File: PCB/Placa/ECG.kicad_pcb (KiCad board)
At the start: 2 copper layers, 60.8 x 24 mm, 59 parts, among them P1 A_CONECTOR_DIN, P2 CONN_01X04, P3 CONN_01X04, P7 Shield, U1 INA333, U2 OPA2335, U3 OPA2335, U4 REF5050, U6 INA333, U7 OPA2335, U8 OPA2335, U9 OPA2335

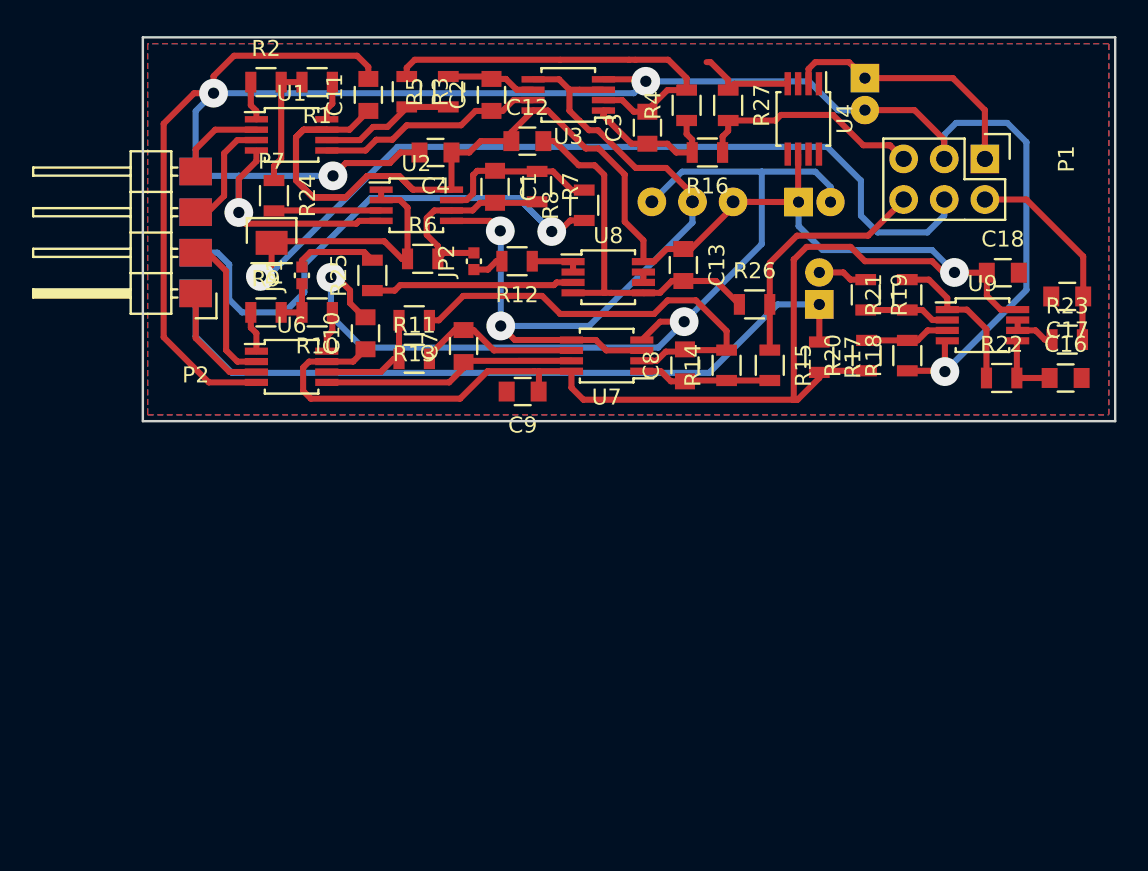
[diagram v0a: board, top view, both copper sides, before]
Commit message: Modifiqué la placa. Le agregué la resistencia para el divisor a la salida del micrófono y cambié la frecuencia del pasabajos a 500Hz aprox, por lo que estuvimos hablando con Mario.
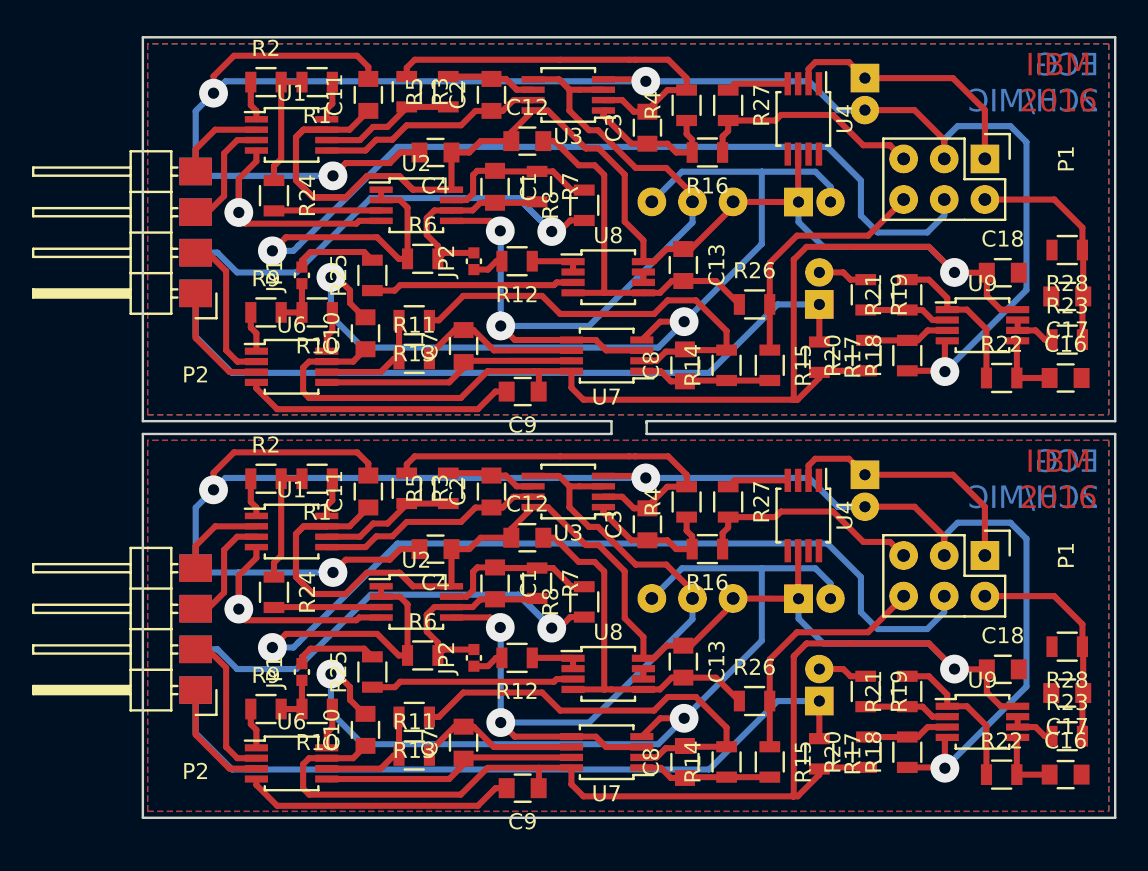
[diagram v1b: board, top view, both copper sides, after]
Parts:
- removed P7: Shield, Pin_Headers:Pin_Header_Straight_1x01
- added C1: 10n, Capacitors_SMD:C_0805, F.Cu at (157.0, 104.7)
- added C10: 0.1u, Capacitors_SMD:C_0805, F.Cu at (148.9, 113.9)
- added C11: 0.1u, Capacitors_SMD:C_0805, F.Cu at (149.1, 99.0)
- added C12: 0.1u, Capacitors_SMD:C_0805, F.Cu at (159.0, 101.9)
- added C13: 0.1u, Capacitors_SMD:C_0805, F.Cu at (168.8, 109.6)
- added C15: 4.7u, Capacitors_ThroughHole:C_Radial_D5_L11_P2, B.Cu at (177.3, 112.1)
- added C16: 0.1u, Capacitors_SMD:C_0805, F.Cu at (192.7, 116.7)
- added C17: 0.1u, Capacitors_SMD:C_0805, F.Cu at (192.8, 111.6)
- added C18: 0.1u, Capacitors_SMD:C_0805, F.Cu at (188.8, 110.1)
- added C2: 1u, Capacitors_SMD:C_0805, F.Cu at (156.8, 99.0)
- added C3: 330n, Capacitors_SMD:C_0805, F.Cu at (166.6, 101.0)
- added C4: 0.1u, Capacitors_SMD:C_0805, F.Cu at (153.3, 102.6)
- added C5: 1u, Capacitors_ThroughHole:C_Radial_D5_L11_P2, B.Cu at (180.2, 98.0)
- added C6: 22u, Capacitors_ThroughHole:C_Radial_D5_L11_P2, B.Cu at (176.0, 105.7)
- added C7: 1u, Capacitors_SMD:C_0805, F.Cu at (155.1, 114.7)
- added C8: 330n, Capacitors_SMD:C_0805, F.Cu at (168.9, 115.9)
- added C9: 0.1u, Capacitors_SMD:C_0805, F.Cu at (158.8, 117.5)
- added JP1: Jumper, jumper_smd:jumper_smd, F.Cu at (144.9, 110.3)
- added JP2: Jumper, jumper_smd:jumper_smd, F.Cu at (155.7, 109.4)
- added P1: A_CONECTOR_DIN, Pin_Headers:Pin_Header_Straight_2x03, F.Cu at (187.7, 103.0)
- added P2: CONN_01X04, Pin_Headers:Pin_Header_Angled_1x04, F.Cu at (138.3, 111.4)
- added P3: CONN_01X04, Pin_Headers:Pin_Header_Angled_1x04, B.Cu at (138.3, 103.8)
- added R1: 12k, Resistors_SMD:R_0805, F.Cu at (145.9, 98.2)
- added R10: 12k, Resistors_SMD:R_0805, F.Cu at (145.9, 112.6)
- added R11: 330k, Resistors_SMD:R_0805, F.Cu at (152.0, 115.5)
- added R12: 10k, Resistors_SMD:R_0805, F.Cu at (158.4, 109.4)
- added R13: 100, Resistors_SMD:R_0805, F.Cu at (152.0, 113.1)
- added R14: 10k, Resistors_SMD:R_0805, F.Cu at (171.5, 115.9)
- added R15: 4,7k, Resistors_SMD:R_0805, F.Cu at (174.2, 115.9)
- added R16: 4,7k, Resistors_SMD:R_0805, F.Cu at (170.3, 102.6)
- added R17: 2.2k, Resistors_SMD:R_0805, F.Cu at (177.3, 115.4)
- added R18: 1.1k, Resistors_SMD:R_0805, F.Cu at (182.8, 115.3)
- added R19: 10k, Resistors_SMD:R_0805, F.Cu at (180.2, 111.5)
- added R2: 12k, Resistors_SMD:R_0805, F.Cu at (142.7, 98.2)
- added R20: 2.2k, Resistors_SMD:R_0805, F.Cu at (180.2, 115.3)
- added R21: 100k, Resistors_SMD:R_0805, F.Cu at (182.8, 111.5)
- added R22: 3.3k, Resistors_SMD:R_0805, F.Cu at (188.7, 116.7)
- added R23: 4.7k, Resistors_SMD:R_0805, F.Cu at (192.8, 114.3)
- added R24: 100k, Resistors_SMD:R_0805, F.Cu at (143.2, 105.3)
- added R25: 100k, Resistors_SMD:R_0805, F.Cu at (149.4, 110.3)
- added R26: 9,1k, Resistors_SMD:R_0805, F.Cu at (173.2, 112.1)
- added R27: 9,1k, Resistors_SMD:R_0805, F.Cu at (171.6, 99.7)
- added R28: 9.1k, Resistors_SMD:R_0805, F.Cu at (192.8, 108.7)
- added R28: 9.1k, Resistors_SMD:R_0805, F.Cu at (192.8, 83.9)
- added R3: 100, Resistors_SMD:R_0805, F.Cu at (151.5, 98.8)
- added R4: 10k, Resistors_SMD:R_0805, F.Cu at (169.0, 99.7)
- added R5: 330k, Resistors_SMD:R_0805, F.Cu at (154.1, 98.8)
- added R6: 10k, Resistors_SMD:R_0805, F.Cu at (152.5, 109.2)
- added R7: 2.2k, Resistors_SMD:R_0805, F.Cu at (159.7, 104.7)
- added R8: 100k, Resistors_SMD:R_0805, F.Cu at (162.6, 105.9)
- added R9: 12k, Resistors_SMD:R_0805, F.Cu at (142.7, 112.6)
- added RV1: 10k, Potentiometers:Potentiometer_Bourns_3296W_3-8Zoll_Inline_ScrewUp, B.Cu at (171.9, 105.7)
- added U1: INA333, Housings_SSOP:MSOP-8_3x3mm_Pitch0.65mm, F.Cu at (144.3, 101.5)
- added U2: OPA2335, Housings_SSOP:MSOP-8_3x3mm_Pitch0.65mm, F.Cu at (152.1, 105.9)
- added U3: OPA2335, Housings_SSOP:MSOP-8_3x3mm_Pitch0.65mm, F.Cu at (161.6, 99.0)
- added U4: REF5050, Housings_SSOP:MSOP-8_3x3mm_Pitch0.65mm, F.Cu at (176.3, 100.5)
- added U6: INA333, Housings_SSOP:MSOP-8_3x3mm_Pitch0.65mm, F.Cu at (144.3, 116.0)
- added U7: OPA2335, Housings_SSOP:MSOP-8_3x3mm_Pitch0.65mm, F.Cu at (164.0, 115.3)
- added U8: OPA2335, Housings_SSOP:MSOP-8_3x3mm_Pitch0.65mm, F.Cu at (164.1, 110.4)
- added U9: OPA2335, Housings_SSOP:MSOP-8_3x3mm_Pitch0.65mm, F.Cu at (187.5, 113.4)
- C16, C17: value 470n -> 0.1u
- R23: value 3.3k -> 4.7k
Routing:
- net GND: track 242.9 -> 465.9 mm, vias 7 -> 14
- net +5V: track 148.9 -> 297.5 mm, vias 1 -> 2
- net /Canales_ECG/SHIELD: track 68.1 -> 129.6 mm, vias 1 -> 2
- net /Canales_ECG/REF: track 51.4 -> 102.9 mm, vias 2 -> 4
- net /Microfono/Mic: track 46.8 -> 93.5 mm
- net Net-(C8-Pad2): track 27.7 -> 55.5 mm
- net /Canales_ECG/RL: track 35.2 -> 61.7 mm, vias 1 -> 2
- net Net-(C3-Pad2): track 25.7 -> 51.3 mm
- net Net-(C7-Pad1): track 16.8 -> 33.7 mm
- net +BATT: track 16.4 -> 32.8 mm
- net /Canales_ECG/OUT_ch1: track 15.9 -> 31.8 mm
- net /Canales_ECG/OUT_ch2: track 15.5 -> 31.0 mm
- net /Microfono/OUT_Mic: track 12.8 -> 27.7 mm
- net Net-(C2-Pad1): track 14.2 -> 28.4 mm
- net Net-(R25-Pad1): track 12.8 -> 25.5 mm
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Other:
- board size 60.8 x 24 mm -> 60.8 x 48.8 mm
- board text added: "ECG 2CH/MIC"
- board text added: "IIBM 2016"
